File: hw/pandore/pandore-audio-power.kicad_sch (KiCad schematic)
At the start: 33 parts, among them U12 NXES2, U13 -, U14 -

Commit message: added power stuff revised M.2 for higher model and added m.2 mounts added power tap terminals
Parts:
- added J22: V12ISO, reekilib_con:Wurth_691137710002, symbol reekilib_con:hdr-1x2
- added J23: AV5, reekilib_con:Wurth_691137710002, symbol reekilib_con:hdr-1x2
- added J24: AV3P3, reekilib_con:Wurth_691137710002, symbol reekilib_con:hdr-1x2
- added R142: ${Resistance}, ${Tolerance}, ${Type}, reekilib_res:RESC2012, symbol reekilib_res:res
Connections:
- net AV3P3: now also J24.1, R142.2; no longer C103.2, C114.2, R72.1, U14.1 (OUT)
- net AV5: now also J23.1
- net V12ISO: now also J22.1
- net VSSISO: now also J22.2, J23.2, J24.2
- new net: C103.2, C114.2, R142.1, R72.1, U14.1 (OUT)

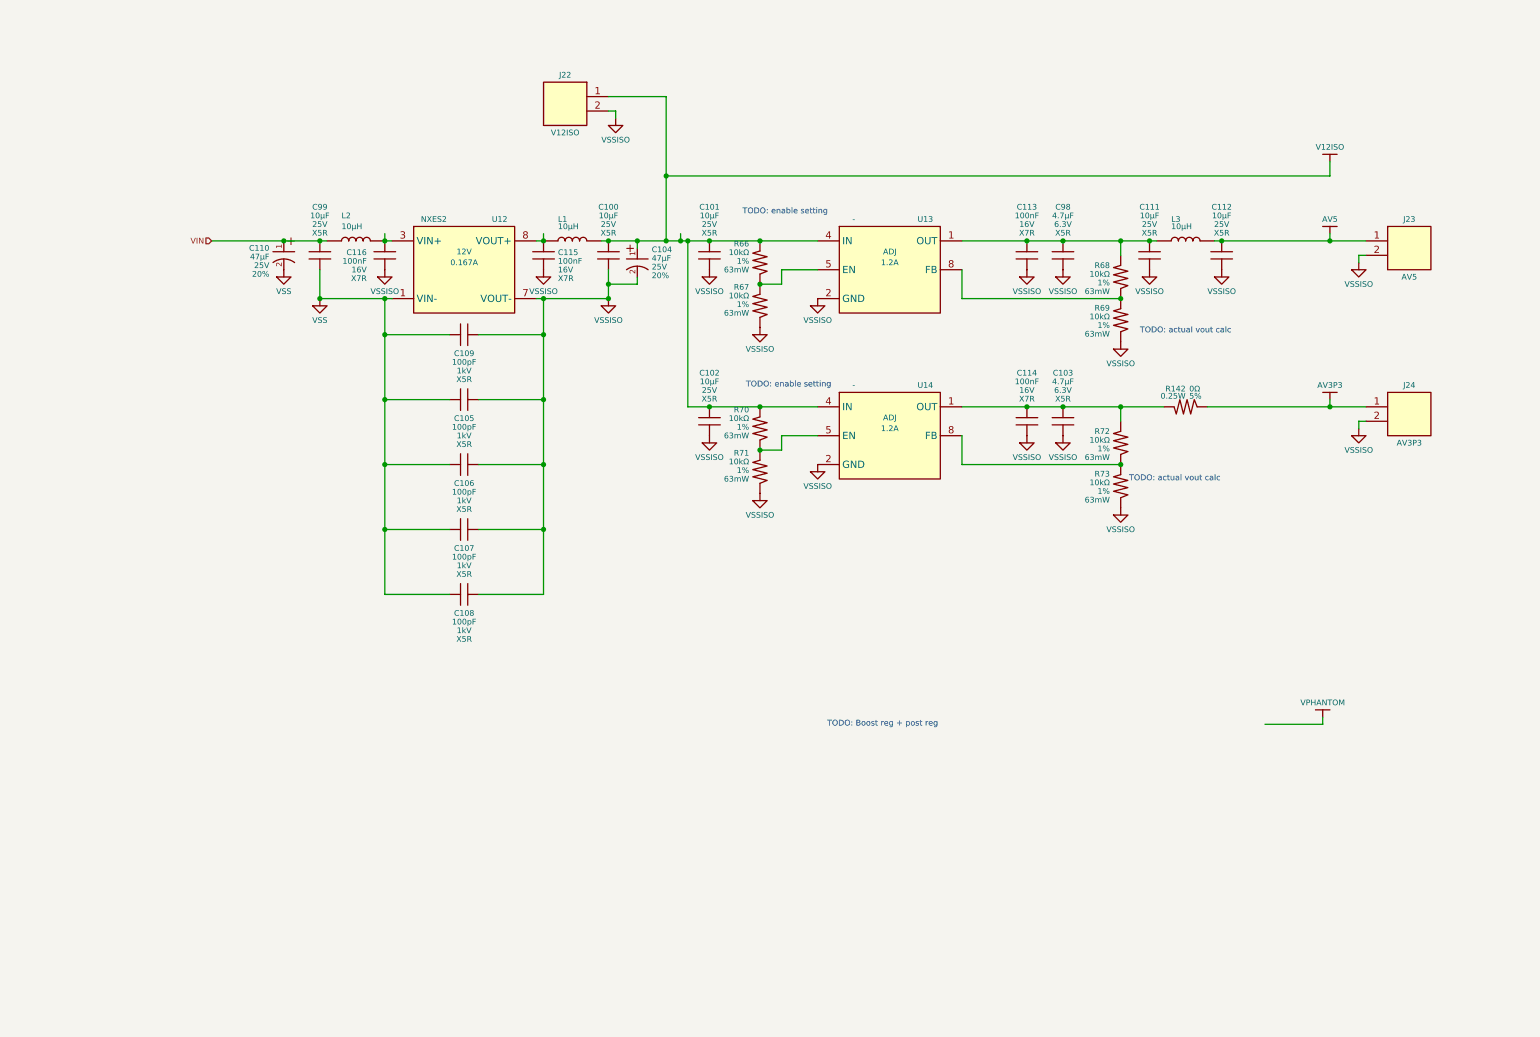
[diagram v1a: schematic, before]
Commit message: Lots of routing done power blocks intra-routing mostly done rp2350 routing mostly done some label cleanup
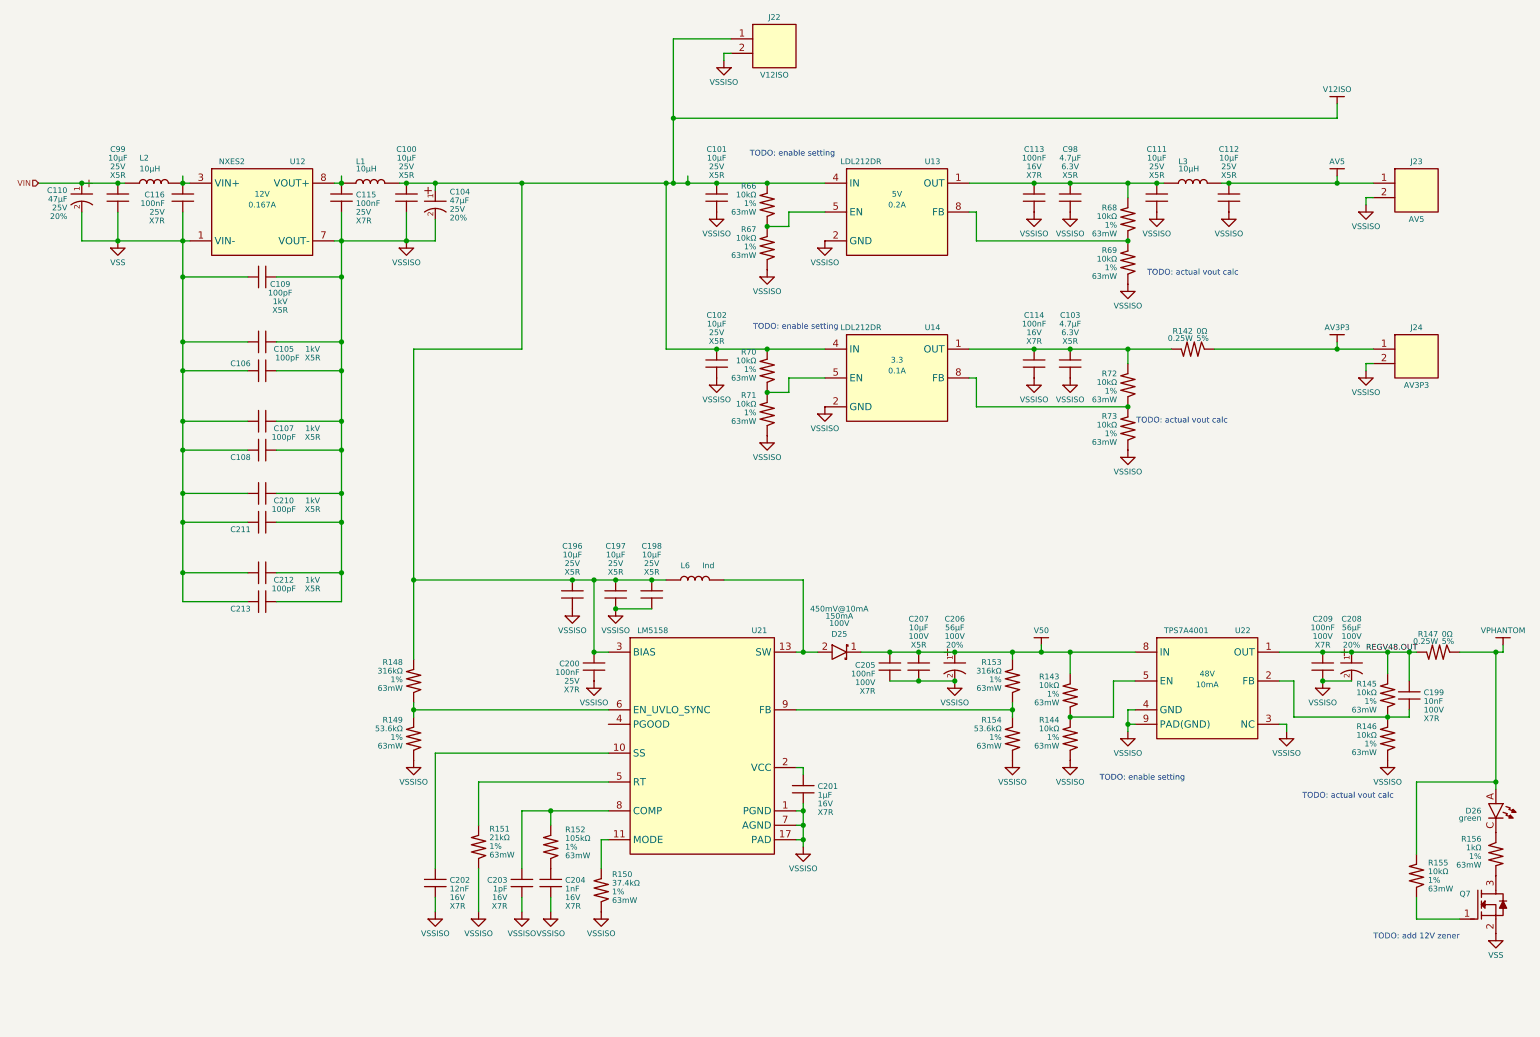
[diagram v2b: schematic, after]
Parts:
- added C196, C197, C198, C205, C209: ${Capacitance}, ${Voltage}, ${Dielectric}, reekilib_cap:CAPC2012, symbol reekilib_cap:cap
- added C199, C200, C202, C203, C204: ${Capacitance}, ${Voltage}, ${Dielectric}, reekilib_cap:CAPC1005, symbol reekilib_cap:cap
- added C201: ${Capacitance}, ${Voltage}, ${Dielectric}, reekilib_cap:CAPC1608, symbol reekilib_cap:cap
- added C206, C208: ${Capacitance}, ${Voltage}, ${Tolerance}, reekilib_cap:CAPAE1000Xxxx, symbol reekilib_cap:cap_pol
- added C207: ${Capacitance}, ${Voltage}, ${Dielectric}, reekilib_cap:CAPC3225, symbol reekilib_cap:cap
- added C210, C211, C212, C213: ${Capacitance}, ${Voltage}, ${Dielectric}, reekilib_cap:CAPC3216, symbol reekilib_cap:cap
- added D25: ${Vr}, ${Io}, ${Vf}, reekilib_sod:sod-123, symbol reekilib_dio:diode_schottky
- added D26: ${color}, reekilib_led:LEDM1608X80, symbol reekilib_led:led
- added L6: Ind, reekilib_ind:WE_IND5030, symbol reekilib_ind:ind
- added Q7: MOSFET_EN-N, reekilib_sot:SOT95P280X100-3, symbol reekilib_mfe:MOSFET_EN-N
- added R143, R144, R145, R146, R148, R149, R150, R151, R152, R153, R154, R155, R156: ${Resistance}, ${Tolerance}, ${Power}, reekilib_res:RESC1005, symbol reekilib_res:res
- added R147: ${Resistance}, ${Tolerance}, ${Type}, reekilib_res:RESC2012, symbol reekilib_res:res
- added U21: LM5158, reekilib_qfn:QFN50P300X300-17, symbol reekilib_swr:LM5158
- added U22: TPS7A4001, reekilib_sop:SOP65P490X300-9, symbol reekilib_ldo:TPS7A4001
- C115, C116: Link https://www.passivecomponent.com/product-search/MLCC/?partn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 -> (none); MFG Walsin Technology Corporation -> (none); MFG2 Samsung Electro-Mechanics -> (none); MFG3 Taiyo Yuden -> (none); MFG4 YAGEO -> (none); MPN 0402B104K160CT -> (none); MPN2 CL05B104KA5NNNC -> (none); MPN3 EMK105B7104KV-F -> (none); MPN4 CC0402KRX7R7BB104 -> (none); Voltage 16V -> 25V
- U13: value - -> LDL212DR; Io 1.2A -> 0.2A; Vo ADJ -> 5V
- U14: value - -> LDL212DR; Io 1.2A -> 0.1A; Vo ADJ -> 3.3
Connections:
- net V12ISO: now also C196.2, C197.2, C198.2, C200.2, L6.1, R148.1, U21.3 (BIAS)
- net VPHANTOM: now also D26.A, R147.2, R155.1
- net VSS: now also C116.1, C210.2, C211.2, C212.2, C213.2, Q7.2 (S)
- net VSSISO: now also C196.1, C197.1, C198.1, C200.1, C201.1, C202.1, C203.1, C204.1, C205.1, C206.2 (-), C207.1, C208.2 (-), C209.1, C210.1, C211.1, C212.1, C213.1, R144.2, R146.2, R149.2, R150.2, R151.2, R154.2, U21.1 (PGND), U21.16 (PGND), U21.17 (PAD), U21.7 (AGND), U22.3 (NC), U22.4 (GND), U22.6 (NC), U22.7 (NC), U22.9 (PAD(GND)); no longer C116.1
- new net: R148.2, R149.1, U21.6 (EN_UVLO_SYNC)
- new net: D25.2 (A), L6.2, U21.13 (SW), U21.14 (SW)
- new net: C199.1, R145.2, R146.1, U22.2 (FB)
- new net: C204.2, R152.2
- new net: R143.2, R144.1, U22.5 (EN)
- new net: Q7.3 (D), R156.1
- new net: D26.C, R156.2
- new net: R153.2, R154.1, U21.9 (FB)
- new net: C203.2, R152.1, U21.8 (COMP)
- new net: Q7.1 (G), R155.2
- new net: R151.1, U21.5 (RT)
- new net: C202.2, U21.10 (SS)
- new net: R150.1, U21.11 (MODE)
- new net: C201.2, U21.2 (VCC)
- new net REGV48.OUT: C199.2, C208.1 (+), C209.2, R145.1, R147.1, U22.1 (OUT)
- new net V50: C205.2, C206.1 (+), C207.2, D25.1 (C), R143.1, R153.1, U22.8 (IN)
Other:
- note added: "TODO: add 12V zener"
- note removed: "TODO: Boost reg + post reg"
- moved on the sheet: C100, C101, C102, C103, C104, C105, C106, C107, C108, C109, C110, C111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

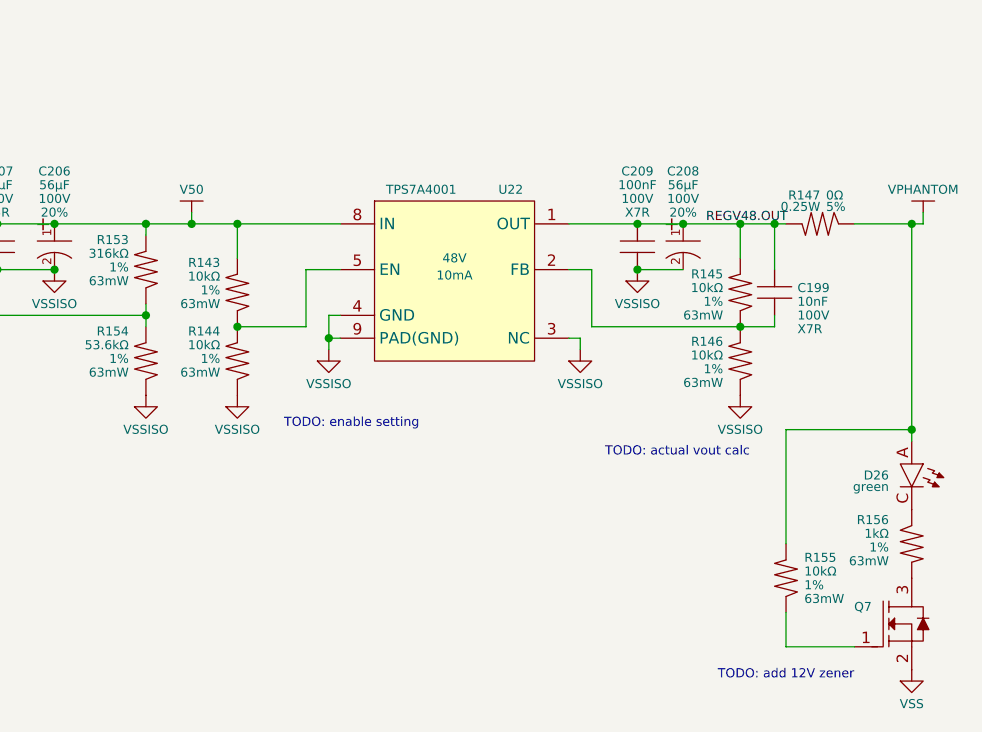
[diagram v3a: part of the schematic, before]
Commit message: lots of routing (diff, buses, power) done optimised buffer out
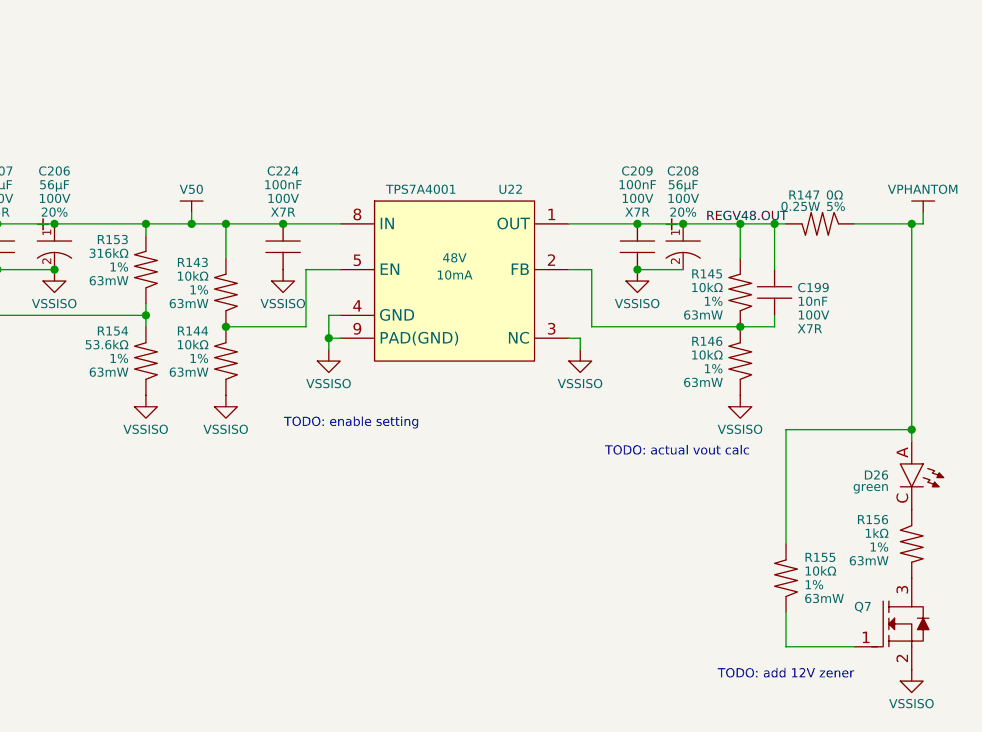
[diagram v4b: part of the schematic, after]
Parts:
- added C224: ${Capacitance}, ${Voltage}, ${Dielectric}, reekilib_cap:CAPC2012, symbol reekilib_cap:cap
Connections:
- net V50: now also C224.2
- net VSS: no longer Q7.2 (S)
- net VSSISO: now also Q7.2 (S), C224.1
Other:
- moved on the sheet: R143, R144

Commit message: added encoder, more routing done, pinout doc added
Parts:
- C199: footprint reekilib_cap:CAPC1005 -> reekilib_cap:CAPC1608
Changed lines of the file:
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@@
 			)
 		)
-		(property "Footprint" "reekilib_cap:CAPC1005"
+		(property "Footprint" "reekilib_cap:CAPC1608"
 			(at 264.16 144.272 0)
 			(do_not_autoplace yes)

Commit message: added todos following review
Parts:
- C105, C106, C107, C108, C210, C211, C212, C213: now not fitted
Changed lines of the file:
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@@
 		(in_bom yes)
 		(on_board yes)
-		(dnp no)
+		(dnp yes)
 		(property "Reference" "C105"
 			(at 66.04 73.66 90)
@@
 		(in_bom yes)
 		(on_board yes)
-		(dnp no)
+		(dnp yes)
 		(property "Reference" "C210"
 			(at 66.04 100.33 90)
@@
 		(in_bom yes)
 		(on_board yes)
-		(dnp no)
+		(dnp yes)
 		(property "Reference" "C211"
 			(at 58.42 105.41 90)
@@
 		(in_bom yes)
 		(on_board yes)
-		(dnp no)
+		(dnp yes)
 		(property "Reference" "C108"
 			(at 58.42 92.71 90)
@@
 		(in_bom yes)
 		(on_board yes)
-		(dnp no)
+		(dnp yes)
 		(property "Reference" "C213"
 			(at 58.42 119.38 90)
@@
 		(in_bom yes)
 		(on_board yes)
-		(dnp no)
+		(dnp yes)
 		(property "Reference" "C212"
 			(at 66.04 114.3 90)
@@
 		(in_bom yes)
 		(on_board yes)
-		(dnp no)
+		(dnp yes)
 		(property "Reference" "C107"
 			(at 66.04 87.63 90)
@@
 		(in_bom yes)
 		(on_board yes)
-		(dnp no)
+		(dnp yes)
 		(property "Reference" "C106"
 			(at 58.42 76.2 90)
